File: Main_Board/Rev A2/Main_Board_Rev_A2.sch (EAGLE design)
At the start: 209 parts, among them J1 90814-0208, J2 90814-0206, J3 90814-0208, K1 G6K-2G-Y, K2 G6K-2G-Y, K3 G6K-2G-Y, K4 G6K-2G-Y, SW1 B3FS-1015, SW2 B3FS-1015, T1 MMBT2222AL, U1 LT1767EMS8E-5PBF, U10 SN74LVC2G17DBVR, U11 MCP2561-E/SN, U12 TLV313, U13 SN74LVC3G17DCTR, U2 TPL0401A, U3 SN74LVC3G17DCTR, U4 SN74LVC3G17DCTR, U5 TC1264-3.3, U6 DP83848JSQ/NOPB, U7 LPC1768FBD100, U8 AT24C512C-SSHM-B, U9 SN74LVC2G17DBVR, X1 22-05-7028-02, X10 22-05-7048-04, X11 5504F1-09S-02A-03, X12 22-05-7028-02, X13 22-05-7028-02, X14 22-05-7038-03, X15 22-05-7038-03, X16 22-05-7048-04, X17 22-05-7048-04, X18 22-05-7058-05, X2 22-27-2061-06, X3 RB1-125BAG1A, X4 MSTBA2, X5 22-05-7028-02, X6 USB3075-30-A, X7 FTSH-105-01-L-DV, X8 22-05-7028-02, X9 1241050-5

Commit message: Update schematic
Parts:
- removed C100: 4.7uF, rcl:CPOL-EUCT3216
- removed C111, C115, C118, C119, C123, C124, C125, C126, C135, C137, C138, C139, C140: 0.1uF, rcl:C-EUC0603
- removed C121: 10uF, rcl:CPOL-EUCT3216
- removed C127, C128: 18pF, rcl:C-EUC0603
- removed C136: 100nF, rcl:C-EUC0603
- removed D1: USB120, diode:USB120
- removed L100: 0603PS-103KLB, coilcraft:0603PS
- removed R100, R101: 0R, rcl:R-EU_R0603
- removed R102, R103: 10K, rcl:R-EU_R0603
- removed R104: 1K2, rcl:R-EU_R0603
- removed R105, R106, R107: 4K7, rcl:R-EU_R0603
- removed R60, R61: 1K, rcl:R-EU_R0603
- removed R62, R66: 100, rcl:R-EU_R0603
- removed SJ1, SJ2, SJ3: SOLDERJUMPERNO, SparkFun-Passives:SOLDERJUMPERNO
- removed TP3: TPB1,27, testpad:TPB1,27
- removed U$1: 3000, keystone:3000
- removed U13: SN74LVC3G17DCTR, ti:SN74LVC3G17DCTR
- removed X10, X16, X17: 22-05-7048-04, con-molex:22-05-7048-04
- removed X11: 5504F1-09S-02A-03, con-multicomp:5504F1-09S-02A-03
- removed X18: 22-05-7058-05, con-molex:22-05-7058-05
- removed X9: 1241050-5, con-amp:1241050-5
- removed XT1: ASE_50, crystal:ASE
- removed XT2: FC-135, crystal:FC-135
- removed XT3: ASE-12, crystal:ASE
- added C22: 100nF, rcl:C-EUC0603
- added C23: 4700pF, rcl:C-EUC0603
- added C24: 22uF, rcl:C-EUC0805
- added C25, C28, C29, C30, C31, C32, C33, C34, C36, C37, C38: 0.1uF, rcl:C-EUC0603
- added C26, C27: 18pF, rcl:C-EUC0603
- added C35: 10uF, rcl:CPOL-EUCT3216
- added D3: MBRS140, diode:MBRS140
- added GND: DP83848JSQ/NOPB, textas:DP83848JSQ/NOPB
- added J12: 22-27-2061-06, con-molex:22-27-2061-06
- added J15: 1241050-5, con-amp:1241050-5
- added J4: 5504F1-09S-02A-03, con-multicomp:5504F1-09S-02A-03
- added J5, J6, J8: 22-05-7048-04, con-molex:22-05-7048-04
- added J7: 22-05-7058-05, con-molex:22-05-7058-05
- added JP6: FIDUCIAL1X2, SparkFun:FIDUCIAL1X2
- added L2: 15uH, Wurth-POWER_MAGNETICS-rev16f:WE-PD2_5848/5820
- added L3: 0603PS-103KLB, coilcraft:0603PS
- added LED10: Blue, led:LEDCHIPLED_0603
- added P1: RB1-125BAG1A, con-wiznet:RB1-125BAG1A
- added R67, R68, R69: 0R, rcl:R-EU_R0603
- added R70: 1K5, rcl:R-EU_R0603
- added R71, R73, R76: 2K7, rcl:R-EU_R0603
- added R72, R74, R75: 1K, rcl:R-EU_R0603
- added R77, R78: 1K8, rcl:R-EU_R0603
- added R79, R80: 1K2, rcl:R-EU_R0603
- added TP5: TPB1,27, testpad:TPB1,27
- C1: MPN (none) -> GRT188R61H225KE13D; OC_NEWARK (none) -> 01AC8938
- C12: value 0.1uF -> 22uF; device rcl:C-EUC0603 -> rcl:C-EUC0805; MPN (none) -> MCMT21N220F250CT; OC_NEWARK (none) -> 23T7233
- C13: value 4700pF -> 100nF; MPN (none) -> MC0603B104K250CT; OC_NEWARK (none) -> 06R4925
- C14, C16, C18, C19, C20, C21, C7, C8: MPN (none) -> MC0603B104K250CT; OC_NEWARK (none) -> 06R4925
- C15, C17: MPN (none) -> F931A106MAA; OC_NEWARK (none) -> 58R3260
- C2: value 0.1uF -> 2.2uF; MPN (none) -> GRT188R61H225KE13D; OC_NEWARK (none) -> 01AC8938
- C3: value 0.1uF -> 1000pF; MPN (none) -> MC0603B102K500CT; OC_NEWARK (none) -> 06R4910
- C4: value 10uF -> 1000pF; device rcl:CPOL-EUCT3216 -> rcl:C-EUC0603; MPN (none) -> MC0603B102K500CT; OC_NEWARK (none) -> 06R4910
- C5, C6: value 1uF -> 2.2uF; MPN (none) -> GRT188R61H225KE13D; OC_FARNELL unknown -> (none); OC_NEWARK (none) -> 01AC8938
- C9: value 100nF -> 4.7uF; device rcl:C-EUC0603 -> rcl:CPOL-EUCT3216; MPN (none) -> F931A475MAA; OC_NEWARK (none) -> 58R3271
- D2: value CMDSH2-3 -> MBRS140; device diode:CMDSH2-3 -> diode:MBRS140; MF (none) -> ON SEMICONDUCTOR; MPN (none) -> MBRS140T3G; OC_NEWARK (none) -> 83H7272
- JP3, SW1, SW2: OC_NEWARK (none) -> unknown
- L1: value 4.7uF -> 10uH; device WE-PD:WE-PD-7447713047_1030/1050 -> Wurth-POWER_MAGNETICS-rev16f:WE-PD2_5848/5820; MPN (none) -> 74477410; OC_NEWARK (none) -> 08P2817
- LED3, LED4: MF MULTICOMP -> (none)
- R1: value 4K7 -> 1k5; MF (none) -> Multicomp Passives; MPN (none) -> MC0063W060311K5; OC_FARNELL (none) -> 2073391; OC_NEWARK (none) -> 58K4488
- R16: value 0R -> 1k5; MF (none) -> Multicomp Passives; MPN (none) -> MC0063W060311K5; OC_FARNELL (none) -> 2073391; OC_NEWARK (none) -> 58K4488
- R17: value 0R -> 4K7; MPN (none) -> MCMR06X4701FTL; OC_NEWARK (none) -> 86T3649
- R18: value 4K7 -> 220; MPN (none) -> MCMR06X2200FTL; OC_NEWARK (none) -> 86T3577
- R19: MPN (none) -> MCMR06X2200FTL; OC_NEWARK (none) -> 86T3577
- R20: value 220 -> 49.9; MPN (none) -> MCMR06X49R9FTL; OC_NEWARK (none) -> 86T3659
- R21, R22, R23: MPN (none) -> MCMR06X49R9FTL; OC_NEWARK (none) -> 86T3659
- R24: value 49.9 -> 4K7; MPN (none) -> MCMR06X4701FTL; OC_NEWARK (none) -> 86T3649
- R27: value 1K5 -> 4K7; MF MULTICOMP -> (none); MPN MCMR06X1501FTL -> MCMR06X4701FTL; OC_FARNELL 2073391 -> (none); OC_NEWARK 58K4488 -> 86T3649
- R28: value 4K7 -> 2K2; MPN (none) -> MCMR06X2201FTL; OC_NEWARK (none) -> 86T3578
- R29, R30: value 4K7 -> 31k6; MF (none) -> Multicomp Passives; MPN (none) -> MC0063W060311K5; OC_FARNELL (none) -> 2073391; OC_NEWARK (none) -> 58K4488
- R31: value 1K5 -> 10k; MF MULTICOMP -> (none); MPN MCMR06X1501FTL -> MCMR06X1002FTL; OC_NEWARK 58K4488 -> 86T3506
- R33: value 4K7 -> 52k3; MPN (none) -> MC0063W0603152K3; OC_FARNELL (none) -> 2073391; OC_NEWARK (none) -> 26M0962
- R49: value 1K2 -> 10k; MPN (none) -> MCMR06X1002FTL; OC_FARNELL (none) -> 2073391; OC_NEWARK (none) -> 86T3506
- R54, R55: MPN (none) -> MCMR06X60R4FTL; OC_NEWARK (none) -> 86T3680
- R56: value 1K8 -> 31k6; MF (none) -> Multicomp Passives; MPN (none) -> MC0063W060311K5; OC_FARNELL (none) -> 2073391; OC_NEWARK (none) -> 58K4488
- R57: value 1K8 -> 4K7; MPN (none) -> MCMR06X4701FTL; OC_NEWARK (none) -> 86T3649
- R58, R59: value 10K -> 1K; MPN (none) -> MCMR06X1001FTL; OC_NEWARK (none) -> 86T3505
- R63, R64: value 100 -> 10K; MPN (none) -> MCMR06X1002FTL; OC_NEWARK (none) -> 86T3506
- R65: value 100 -> 0R; MPN (none) -> MCMR06X000 PTL; OC_NEWARK (none) -> 86T3500
- U1: value LT1767EMS8E-5PBF -> LT3686HDDPBF; device lineartechnology:LT1767EMS8E-5PBF -> lineartechnology:LT3686HDDPBF
- U11: MPN (none) -> MCP2561-E/SN; OC_NEWARK (none) -> 12X8698
- U12: MPN (none) -> TLV313IDBVT; OC_NEWARK (none) -> 95Y0395
- U5: value TC1264-3.3 -> LT3686HDDPBF; device microchip-6:TC1264-3.3 -> lineartechnology:LT3686HDDPBF; OC_FARNELL unknown -> (none)
- U6: value DP83848JSQ/NOPB -> LPC1768FBD100; device texas:DP83848JSQ/NOPB -> NXP:LPC1768FBD100; MPN (none) -> LPC1768FBD100; OC_NEWARK (none) -> 15R1840
- U7: value LPC1768FBD100 -> AT24C512C-SSHM-B; device NXP:LPC1768FBD100 -> atmel:AT24C512C-SSHM-B
- U8: value AT24C512C-SSHM-B -> SN74LVC3G17DCTR; device atmel:AT24C512C-SSHM-B -> ti:SN74LVC3G17DCTR; MF (none) -> TEXAS INSTRUMENTS
- X1: value 22-05-7028-02 -> ASE_50; device con-molex:22-05-7028-02 -> crystal:ASE; MPN (none) -> ASE-50.000MHZ-LC-T; OC_NEWARK (none) -> 84R2105
- X2: value 22-27-2061-06 -> FC-135; device con-molex:22-27-2061-06 -> crystal:FC-135; MPN (none) -> Q13FC13500004; OC_NEWARK (none) -> 31M4970
- X3: value RB1-125BAG1A -> ASE-12; device con-wiznet:RB1-125BAG1A -> crystal:ASE; MPN (none) -> ASE-12.000MHZ-LC-T; OC_NEWARK (none) -> 40Y2118
- X7: value FTSH-105-01-L-DV -> 3000; device con-samtec:FTSH-105-01-L-DV -> keystone:3000; MF (none) -> KEYSTONE ELECTR; MPN (none) -> 3000; OC_NEWARK (none) -> 66F5622
- renumbered C110 to C15, C112 to C20, C113 to C19, C114 to C16, C116 to C14, C117 to C18, C120 to C21, C122 to C17
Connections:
- removed net CAN_H: R54.2, U11.CANH, X11C.7
- removed net CAN_L: R55.1, U11.CANL, X11C.2
- removed net ETH_RXD_N: U6.RXD_1/PHYAD2, U7.P1[9]/ENET_RXD0
- removed net ETH_RXD_P: U6.RXD_0/PHYAD1, U7.P1[10]/ENET_RXD1
- removed net ETH_TXD_N: U6.TXD_0, U7.P1[0]/ENET_TXD0
- removed net ETH_TXD_P: U6.TXD_1, U7.P1[1]/ENET_TXD1
- removed net N$67: R104.2, R56.2, U12.-IN
- removed net N$68: R56.1, X10-3.S
- removed net N$69: SJ1.1, X2-2.S
- removed net RESET: R103.1, R16.1, SW1.1, U7.*RESET, X7-10.S, X9.P$5
- new net !JTAG_TRST: J15.P$5, U6.*TRST
- new net !RESET: R63.1, R65.1, SW1.1, U6.*RESET
- new net CAN_N: J4C.2, R55.1, U11.CANL
- new net CAN_P: J4C.7, R54.2, U11.CANH
- new net ETH_RXD_0: GND.RXD_0/PHYAD1, U6.P1[9]/ENET_RXD0
- new net ETH_RXD_1: GND.RXD_1/PHYAD2, U6.P1[10]/ENET_RXD1
- new net ETH_TXD_0: GND.TXD_0, U6.P1[0]/ENET_TXD0
- new net ETH_TXD_1: GND.TXD_1, U6.P1[1]/ENET_TXD1
- new net LED_DEBUG: LED10.A, U6.P1[21]/*MCABORT/PWM1[3]/SSEL0
- new net N$10: R30.2, U1.RT
- new net N$30: R31.2, R33.1, U5.FB
- new net N$34: C5.2, D2.C, L2.1, U5.SW
- new net N$36: R49.2, R56.1, U1.FB
- new net N$78: J8-3.S, R78.1
- new net N$79: R77.2, R79.2, U12.+IN
- new net N$80: R78.2, R80.2, U12.-IN
- net +24V: now also C2.1, J4C.9, J5-1.S, J6-1.S, U1.EN/UVLO, U5.EN/UVLO, U5.VIN; no longer X11C.9, X16-1.S, X17-1.S
- net +3V3: now also C22.1, C25.1, C29.1, C30.1, C31.1, C32.1, C33.1, C34.1, C35.+, C36.1, C37.1, C38.1, C9.+, GND.AVDD33, GND.IOVDD33, GND.IOVDD33_2, J15.P$1, L1.2, L3.1, P1.CT, R1.2, R17.2, R18.2, R20.1, R27.2, R56.2, R57.2, R63.2, R64.2, TP5.TP, U1.BD, U6.NC, U6.VDD, U6.VDD_2, U6.VDD_3, U6.VDD_4, U6.VDD_5, U6.VDD_6, U7.VCC, X1.TRI, X1.VDD, X3.TRI, X3.VDD; no longer C100.+, C111.1, C115.1, C118.1, C119.1, C121.+, C123.1, C124.1, C125.1, C135.1, C136.1, C137.1, C6.1, C9.1, L100.1, R102.2, R103.2, R20.2, R24.1, R29.2, R30.2, R31.2, R33.2, R58.2, R59.2, TP3.TP, U11.VDD, U13.VCC, U5.VOUT, U6.AVDD33, U6.IOVDD33, U6.IOVDD33_2, U7.NC, U7.VDD, U7.VDD_2, U7.VDD_3, U7.VDD_4, U7.VDD_5, U7.VDD_6, X3.CT, X7-1.S, X9.P$1, XT1.TRI, XT1.VDD, XT3.TRI, XT3.VDD
- net +5V: now also C13.1, C24.1, J7-4.S, J8-1.S, L2.2, R16.2, R33.2, R71.1, R73.1, R76.1, U11.VDD, U5.BD; no longer C4.+, C5.1, D2.A, L1.2, R105.1, R106.1, R107.1, R27.2, SJ1.2, U1.FB, U5.VIN, X1-1.S, X10-1.S, X18-1.S
- net ADC_SLACK_DETECTION: now also R80.1, U6.P0[25]/AD0[2]/I2SRX_SDA/TXD3; no longer R49.1, U7.P0[25]/AD0[2]/I2SRX_SDA/TXD3
- net ADC_TEMP_0: now also U6.P0[23]/AD0[0]/I2SRX_CLK/CAP3[0]; no longer U7.P0[23]/AD0[0]/I2SRX_CLK/CAP3[0]
- net ADC_TEMP_1: now also U6.P0[24]/AD0[1]/I2SRX_WS/CAP3[1]; no longer U7.P0[24]/AD0[1]/I2SRX_WS/CAP3[1]
- net AVDD: now also C28.1, L3.2, U6.VDDA, U6.VREFP; no longer C126.1, L100.2, U7.VDDA, U7.VREFP
- net BOOT_SELECT_P2_10: now also R68.1, U6.P2[10]/*EINT0/NMI; no longer R100.1, U7.P2[10]/*EINT0/NMI
- net BOOT_SELECT_P2_12: now also R69.1, U6.P2[12]/*EINT2/I2STX_WS; no longer R101.1, U7.P2[12]/*EINT2/I2STX_WS
- net BRAKE_SENSOR_1: now also U6.P0[4]/I2SRX_CLK/RD2/CAP2[0]; no longer U7.P0[4]/I2SRX_CLK/RD2/CAP2[0]
- net BRAKE_SENSOR_2: now also U6.P0[5]/I2SRX_WS/TD2/CAP2[1]; no longer U7.P0[5]/I2SRX_WS/TD2/CAP2[1]
- net CAN_RX: now also U6.P0[0]/RD1/TXD3/SDA1; no longer U7.P0[0]/RD1/TXD3/SDA1
- net CAN_SHLD: now also J4C.5; no longer X11C.5
- net CAN_SPLIT: now also C23.2; no longer C13.2
- net CAN_TX: now also U6.P0[1]/TD1/RXD3/SCL1; no longer U7.P0[1]/TD1/RXD3/SCL1
- net DRIVE_EN: now also U6.P0[6]/I2SRX_SDA/SSEL1/MAT2[0]; no longer U7.P0[6]/I2SRX_SDA/SSEL1/MAT2[0]
- net DRIVE_ERR: now also U6.P0[7]/I2STX_CLK/SCK1/MAT2[1]; no longer U7.P0[7]/I2STX_CLK/SCK1/MAT2[1]
- net EEPROM_SCL: now also R27.1, U6.P0[28]/SCL0/USB_SCL, U7.SCL; no longer R30.1, U7.P0[28]/SCL0/USB_SCL, U8.SCL
- net EEPROM_SDA: now also R17.1, U6.P0[27]/SDA0/USB_SDA, U7.SDA; no longer R33.1, U7.P0[27]/SDA0/USB_SDA, U8.SDA
- net ENCODER_A: now also U6.P1[20]/MCI0/PWM1[2]/SCK0, U8.1Y; no longer U13.1Y, U7.P1[20]/MCI0/PWM1[2]/SCK0
- net ENCODER_B: now also U6.P1[23]/MCI1/PWM1[4]/MISO0, U8.2Y; no longer U13.2Y, U7.P1[23]/MCI1/PWM1[4]/MISO0
- net ENCODER_Z: now also U6.P1[24]/MCI2/PWM1[5]/MOSI0, U8.3Y; no longer U13.3Y, U7.P1[24]/MCI2/PWM1[5]/MOSI0
- net ETH_CLK_EN: now also U6.P1[27]/CLKOUT/*USB_OVRCR/CAP0[1]; no longer U7.P1[27]/CLKOUT/*USB_OVRCR/CAP0[1]
- net ETH_CRS: now also GND.CRS/CRS_DV/LED_CFG, U6.P1[8]/ENET_CRS; no longer U6.CRS/CRS_DV/LED_CFG, U7.P1[8]/ENET_CRS
- net ETH_MDC: now also GND.MDC, U6.P1[16]/ENET_MDC; no longer U6.MDC, U7.P1[16]/ENET_MDC
- net ETH_MDIO: now also GND.MDIO, U6.P1[17]/ENET_MDIO; no longer U6.MDIO, U7.P1[17]/ENET_MDIO
- net ETH_RST: now also GND.RESET_N, U6.P1[28]/MCOA2/PCAP1[0]/MAT0[0]; no longer U6.RESET_N
- net ETH_RX_ER: now also GND.RX_ER/MDIX_EN, U6.P1[14]/ENET_RX_ER; no longer U6.RX_ER/MDIX_EN, U7.P1[14]/ENET_RX_ER
- net ETH_RX_N: now also GND.RD-, P1.RD-, R23.2; no longer R24.2, U6.RD-, X3.RD-
- net ETH_RX_P: now also GND.RD+, P1.RD+, R22.2; no longer R23.2, U6.RD+, X3.RD+
- net ETH_TXD_EN: now also GND.TX_EN, U6.P1[4]/ENET_TX_EN; no longer U6.TX_EN, U7.P1[4]/ENET_TX_EN
- net ETH_TX_N: now also GND.TD-, P1.TD-, R21.2; no longer R22.2, U6.TD-, X3.TD-
- net ETH_TX_P: now also GND.TD+, P1.TD+, R20.2; no longer R21.2, U6.TD+, X3.TD+
- net ETH_X1: now also GND.X1, U6.P1[15]/ENET_REF_CLK, X1.OUT; no longer U6.X1, XT1.OUT
- net FAN_1_PWM: now also R58.2, U6.P2[0]/PWM1[1]/TXD1; no longer R61.2, U7.P2[0]/PWM1[1]/TXD1
- net FAN_1_SENSOR: now also U6.P0[8]/I2STX_WS/MISO1/MAT2[2]; no longer R59.1, R62.2
- net FAN_2_PWM: now also R59.2, U6.P2[1]/PWM1[2]/RXD1; no longer R60.2, U7.P2[1]/PWM1[2]/RXD1
- net FAN_2_SENSOR: now also U6.P0[9]/I2STX_SDA/MOSI1/MAT2[3]; no longer R58.1, R66.2
- net GND: now also C13.2, C2.2, C22.2, C24.2, C25.2, C26.2, C27.2, C28.2, C29.2, C3.2, C30.2, C31.2, C32.2, C33.2, C34.2, C35.-, C36.2, C37.2, C38.2, C4.2, C9.-, GND.AGND, GND.AGND_2, GND.DAP, GND.DGND, GND.IOGND, J12-1.S, J15.P$2, J4C.3, J4C.6, J5-4.S, J6-4.S, J7-1.S, J8-4.S, P1.R4, P1.R5, P1.R6, R24.2, R29.1, R30.1, R31.1, R49.1, R70.2, R79.1, U1.EP, U1.MODE, U5.EP, U5.MODE, U6.VREFN, U6.VSS, U6.VSSA, U6.VSS_2, U6.VSS_3, U6.VSS_4, U6.VSS_5, U6.VSS_6, U7.A0, U7.A1, U7.A2, U7.GND, X1.GND, X3.GND, X7.VBAT-; no longer C100.-, C111.2, C115.2, C118.2, C119.2, C121.-, C123.2, C124.2, C125.2, C126.2, C127.2, C128.2, C135.2, C136.2, C137.2, C138.2, C139.2, C140.2, C4.-, C5.2, C6.2, C9.2, D1.A, R1.1, R104.1, R18.2, SJ2.2, SJ3.2, U$1.VBAT-, U1.GND, U1.GND_2, U1.SYNC, U13.GND, U5.GND, U5.GND_2, U6.AGND, U6.AGND_2, U6.DAP, U6.DGND, U6.IOGND, U7.VREFN, U7.VSS, U7.VSSA, U7.VSS_2, U7.VSS_3, U7.VSS_4, U7.VSS_5, U7.VSS_6, U8.A0, U8.A1, U8.A2, X1-2.S, X10-4.S, X11C.3, X11C.6, X16-4.S, X17-4.S, X2-1.S, X3.R4, X3.R5, X3.R6, X7-3.S, X7-5.S, X7-9.S, X9.P$2, XT1.GND, XT3.GND
- net HMI_BUTTON_CPU_1: now also U6.P0[16]/RXD1/SSEL0/SSEL; no longer U7.P0[16]/RXD1/SSEL0/SSEL
- net HMI_BUTTON_CPU_2: now also U6.P0[15]/TXD1/SCK0/SCK; no longer U7.P0[15]/TXD1/SCK0/SCK
- net HMI_BUTTON_CPU_3: now also U6.P0[17]/CTS1/MISO0/MISO; no longer U7.P0[17]/CTS1/MISO0/MISO
- net HMI_BUTTON_CPU_4: now also U6.P0[18]/DCD1/MOSI0/MOSI; no longer U7.P0[18]/DCD1/MOSI0/MOSI
- net HMI_BUTTON_CPU_5: now also U6.P0[19]/DSR1/SDA1; no longer U7.P0[19]/DSR1/SDA1
- net HMI_BUTTON_CPU_6: now also R65.2, R67.1; no longer R16.2, R17.1
- net HMI_BUTTON_MCU_FCT_6: now also R67.2, U6.P0[20]/DTR1/SCL1; no longer R17.2, U7.P0[20]/DTR1/SCL1
- net HMI_LCD_BACKLIGHT: now also U6.P0[22]/RTS1/TD1; no longer U7.P0[22]/RTS1/TD1
- net HMI_LCD_SCL: now also U6.P0[11]/RXD2/SCL2/MAT3[1]; no longer U7.P0[11]/RXD2/SCL2/MAT3[1]
- net HMI_LCD_SDA: now also U6.P0[10]/TXD2/SDA2/MAT3[0]; no longer U7.P0[10]/TXD2/SDA2/MAT3[0]
- net HMI_LED_1: now also U6.P2[2]/PWM1[3]/CTS1/TRACEDATA[3]; no longer U7.P2[2]/PWM1[3]/CTS1/TRACEDATA[3]
- net HMI_LED_2: now also U6.P2[3]/PWM1[4]/DCD1/TRACEDATA[2]; no longer U7.P2[3]/PWM1[4]/DCD1/TRACEDATA[2]
- net HMI_LED_3: now also U6.P2[4]/PWM1[5]/DSR1/TRACEDATA[1]; no longer U7.P2[4]/PWM1[5]/DSR1/TRACEDATA[1]
- net HMI_LED_4: now also U6.P2[5]/PWM1[6]/DTR1/TRACEDATA[0]; no longer U7.P2[5]/PWM1[6]/DTR1/TRACEDATA[0]
- net ISP_RXDO: now also J12-4.S, J15.P$3, U6.P0[3]/RXD0/AD0[6]; no longer U7.P0[3]/RXD0/AD0[6], X2-4.S
- net ISP_TXDO: now also J12-5.S, J15.P$4, U6.P0[2]/TXD0/AD0[7]; no longer U7.P0[2]/TXD0/AD0[7], X2-5.S
- net JTAG_TCK: now also J15.P$8, U6.TCK/SWDCLK; no longer U7.TCK/SWDCLK, X7-4.S, X9.P$8
- net JTAG_TDI: now also J15.P$7, U6.TDI; no longer U7.TDI, X7-8.S, X9.P$7
- net JTAG_TDO: now also J15.P$9, U6.TDO/SWO; no longer U7.TDO/SWO, X7-6.S, X9.P$9
- net JTAG_TMS: now also J15.P$10, U6.TMS/SWDIO; no longer U7.TMS/SWDIO, X7-2.S, X9.P$10
- net L1_1: now also GND.LED_LINK/AN0, P1.L2; no longer U6.LED_LINK/AN0, X3.L2
- net L1_2: now also GND.LED_SPEED/AN1, P1.L4; no longer U6.LED_SPEED/AN1, X3.L4
- net MII_MODE: now also GND.RX_DV/MII_MODE; no longer U6.RX_DV/MII_MODE
- net N$11: now also J5-2.S, R58.1; no longer R61.1, X17-2.S
- net N$12: now also J7-3.S, R71.2, R72.1; no longer R66.1, X16-3.S
- net N$13: now also J6-2.S, R59.1; no longer R60.1, X16-2.S
- net N$14: now also J7-5.S, R74.1, R76.2; no longer R62.1, X17-3.S
- net N$15: no longer R38.2
- net N$16: now also R38.2
- net N$22: now also C4.1, U1.SS; no longer JP3.1, R29.1, U8.WP
- net N$3: now also C23.1; no longer C13.1
- net N$31: now also C5.1, U5.BOOST; no longer R57.1, X10-2.S
- net N$35: now also D2.A, U5.DA; no longer R107.2, R63.1, X18-2.S
- net N$4: now also GND.RBIAS, R24.1; no longer R18.1, U6.RBIAS
- net N$40: now also C6.1, U1.BOOST; no longer R106.2, R64.1, X18-3.S
- net N$43: now also C6.2, D3.C, L1.1, U1.SW; no longer C2.2, D2.C, U1.BOOST
- net N$46: now also D3.A, U1.DA; no longer R105.2, R65.1, X18-4.S
- net N$47: now also JP3.1, R57.1, U7.WP; no longer C3.1, R1.2
- net N$48: now also R64.1, R68.2, R69.2, SW2.1; no longer C3.2, U1.VC
- net N$49: now also LED10.C, R70.1; no longer C2.1, D1.C, L1.1, U1.SW
- net N$5: now also R29.2, U5.RT; no longer R100.2, R101.2, R102.1, SW2.1
- net N$50: now also R1.1; no longer R31.1
- net N$51: now also R16.1; no longer R27.1
- net N$52: now also J7-2.S, R73.2, R75.1; no longer C138.1, R65.2, U13.3A
- net N$53: now also R75.2, U8.3A; no longer C139.1, R64.2, U13.2A
- net N$54: now also R74.2, U8.2A; no longer C140.1, R63.2, U13.1A
- net N$6: now also C3.1, U5.SS; no longer SJ2.1, SJ3.1, X11S.SHIELD
- net N$61: now also R72.2, U8.1A; no longer R49.2, R57.2, U12.+IN
- net N$62: now also J8-2.S, R77.1; no longer X18-5.S
- net N$8: now also P1.L1, R19.1; no longer R20.1, X3.L1
- net N$9: now also P1.L3, R18.1; no longer R19.1, X3.L3
- net PFBOUT: now also GND.PFBIN1, GND.PFBIN2, GND.PFBOUT; no longer U6.PFBIN1, U6.PFBIN2, U6.PFBOUT
- net RTCX1: now also C26.1, U6.RTCX1, X2.1; no longer C127.1, U7.RTCX1, XT2.1
- net RTCX2: now also C27.1, U6.RTCX2, X2.2; no longer C128.1, U7.RTCX2, XT2.2
- net USB_D_N: now also R36.2, U6.P0[30]/USB_D?; no longer R35.2, U7.P0[30]/USB_D?
- net USB_D_P: now also R35.2, U6.P0[29]/USB_D+; no longer R36.2, U7.P0[29]/USB_D+
- net USB_UP_LED: now also U6.P1[18]/USB_UP_LED/PWM1[1]/CAP1[0]; no longer U7.P1[18]/USB_UP_LED/PWM1[1]/CAP1[0]
- net USB_V_BUS: now also U6.P1[30]/VBUS/AD0[4]; no longer U7.P1[30]/VBUS/AD0[4]
- net VBAT+: now also U6.VBAT, X7.VBAT+; no longer U$1.VBAT+, U7.VBAT
- net XTAL1: now also U6.XTAL1, X3.OUT; no longer U7.XTAL1, XT3.OUT
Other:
- note removed: "UART"

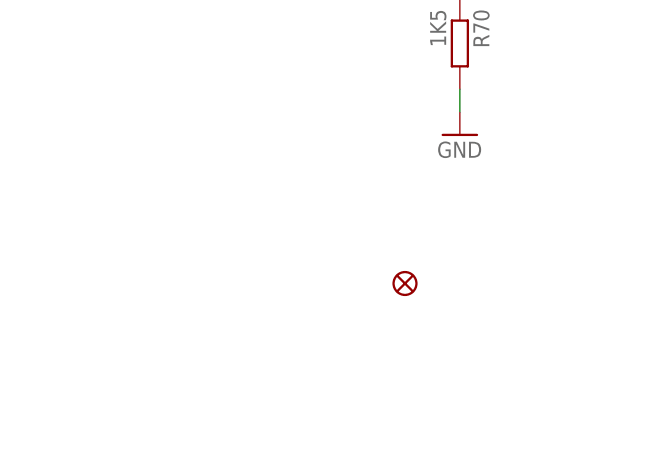
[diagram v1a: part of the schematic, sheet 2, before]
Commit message: Place component on the board
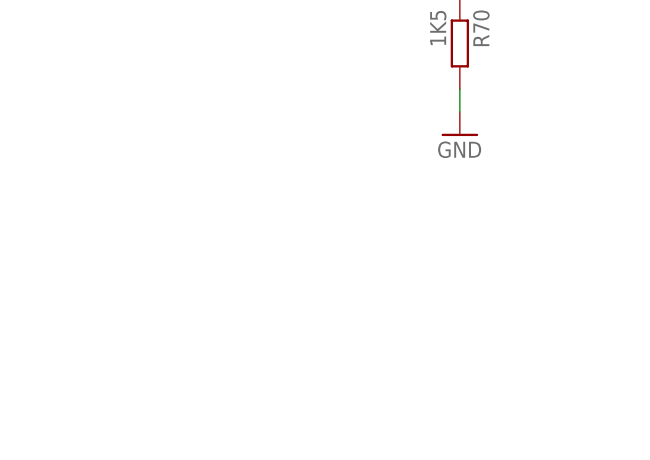
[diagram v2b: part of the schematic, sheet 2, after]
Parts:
- removed JP6: FIDUCIAL1X2, SparkFun:FIDUCIAL1X2
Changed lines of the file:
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@@
 </part>
 <part name="GND87" library="supply1" deviceset="GND" device=""/>
-<part name="JP6" library="SparkFun" deviceset="FIDUCIAL" device="1X2">
-<attribute name="MF" value=""/>
-<attribute name="MPN" value=""/>
-<attribute name="OC_NEWARK" value="unknown"/>
-</part>
 <part name="J12" library="con-molex" deviceset="22-?-06" device="27-2061">
 <attribute name="MF" value="MOLEX"/>
@@
 </instance>
 <instance part="GND87" gate="1" x="358.14" y="35.56"/>
-<instance part="JP6" gate="G$1" x="352.044" y="19.05">
-<attribute name="OC_NEWARK" x="352.044" y="19.05" size="1.778" layer="96" display="off"/>
-<attribute name="MF" x="352.044" y="19.05" size="1.778" layer="96" display="off"/>
-<attribute name="MPN" x="352.044" y="19.05" size="1.778" layer="96" display="off"/>
-</instance>
 </instances>
 <busses>

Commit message: Route Ethernet on the main board
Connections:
- removed net FAN_1_SENSOR: U6.P0[8]/I2STX_WS/MISO1/MAT2[2]
- removed net FAN_2_SENSOR: U6.P0[9]/I2STX_SDA/MOSI1/MAT2[3]
- net FAN_1_PWM: now also U6.P3[25]/MAT0[0]/PWM1[2]; no longer U6.P2[0]/PWM1[1]/TXD1
- net FAN_2_PWM: now also U6.P3[26]/STCLK/MAT0[1]/PWM1[3]; no longer U6.P2[1]/PWM1[2]/RXD1
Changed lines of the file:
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@@
 <net name="FAN_1_PWM" class="1">
 <segment>
-<pinref part="U6" gate="A" pin="P2[0]/PWM1[1]/TXD1"/>
-<wire x1="317.5" y1="167.64" x2="322.58" y2="167.64" width="0.1524" layer="91"/>
-<label x="322.58" y="167.64" size="1.27" layer="95" xref="yes"/>
+<wire x1="134.62" y1="165.1" x2="127" y2="165.1" width="0.1524" layer="91"/>
+<label x="127" y="165.1" size="1.27" layer="95" rot="R180" xref="yes"/>
+<pinref part="U6" gate="A" pin="P3[25]/MAT0[0]/PWM1[2]"/>
 </segment>
 </net>
 <net name="FAN_2_PWM" class="1">
 <segment>
-<pinref part="U6" gate="A" pin="P2[1]/PWM1[2]/RXD1"/>
-<wire x1="317.5" y1="165.1" x2="322.58" y2="165.1" width="0.1524" layer="91"/>
-<label x="322.58" y="165.1" size="1.27" layer="95" xref="yes"/>
-<wire x1="317.5" y1="165.1" x2="322.58" y2="165.1" width="0.1524" layer="91"/>
+<label x="127" y="167.64" size="1.27" layer="95" rot="R180" xref="yes"/>
+<wire x1="132.08" y1="167.64" x2="127" y2="167.64" width="0.1524" layer="91"/>
+<pinref part="U6" gate="A" pin="P3[26]/STCLK/MAT0[1]/PWM1[3]"/>
+<wire x1="132.08" y1="167.64" x2="134.62" y2="167.64" width="0.1524" layer="91"/>
 </segment>
 </net>
@@
 </segment>
 </net>
-<net name="FAN_1_SENSOR" class="1">
-<segment>
-<pinref part="U6" gate="A" pin="P0[8]/I2STX_WS/MISO1/MAT2[2]"/>
-<wire x1="317.5" y1="172.72" x2="322.58" y2="172.72" width="0.1524" layer="91"/>
-<label x="322.58" y="172.72" size="1.27" layer="95" xref="yes"/>
-</segment>
-</net>
-<net name="FAN_2_SENSOR" class="1">
-<segment>
-<pinref part="U6" gate="A" pin="P0[9]/I2STX_SDA/MOSI1/MAT2[3]"/>
-<wire x1="317.5" y1="170.18" x2="322.58" y2="170.18" width="0.1524" layer="91"/>
-<label x="322.58" y="170.18" size="1.27" layer="95" xref="yes"/>
-</segment>
-</net>

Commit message: Route CAN
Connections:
- net CAN_RX renamed CAN_X_N
- net CAN_TX renamed CAN_X_P
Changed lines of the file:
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@@
 </segment>
 </net>
-<net name="CAN_RX" class="1">
+<net name="CAN_X_N" class="1">
 <segment>
 <pinref part="U11" gate="G$1" pin="RXD"/>
@@
 </segment>
 </net>
-<net name="CAN_TX" class="1">
+<net name="CAN_X_P" class="1">
 <segment>
 <pinref part="U11" gate="G$1" pin="TXD"/>
@@
 </busses>
 <nets>
-<net name="CAN_RX" class="1">
+<net name="CAN_X_N" class="1">
 <segment>
 <pinref part="U6" gate="A" pin="P0[0]/RD1/TXD3/SDA1"/>
@@
 </segment>
 </net>
-<net name="CAN_TX" class="1">
+<net name="CAN_X_P" class="1">
 <segment>
 <pinref part="U6" gate="A" pin="P0[1]/TD1/RXD3/SCL1"/>

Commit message: Route the board
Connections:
- net +3V3: now also LED10.A
- net ADC_SLACK_DETECTION: now also U6.P0[23]/AD0[0]/I2SRX_CLK/CAP3[0]; no longer U6.P0[25]/AD0[2]/I2SRX_SDA/TXD3
- net ADC_TEMP_0: now also U6.P0[25]/AD0[2]/I2SRX_SDA/TXD3; no longer U6.P0[23]/AD0[0]/I2SRX_CLK/CAP3[0]
- net GND: no longer R70.2
- net LED_DEBUG: now also R70.2; no longer LED10.A
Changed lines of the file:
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@@
 <attribute name="OC_NEWARK" value="86T3542"/>
 </part>
-<part name="GND87" library="supply1" deviceset="GND" device=""/>
 <part name="J12" library="con-molex" deviceset="22-?-06" device="27-2061">
 <attribute name="MF" value="MOLEX"/>
@@
 <part name="GND97" library="supply1" deviceset="GND" device=""/>
 <part name="+3V28" library="supply1" deviceset="+3V3" device=""/>
+<part name="+3V14" library="supply1" deviceset="+3V3" device=""/>
 </parts>
 <sheets>
@@
 <attribute name="MPN" x="358.14" y="45.72" size="1.778" layer="96" display="off"/>
 </instance>
-<instance part="GND87" gate="1" x="358.14" y="35.56"/>
+<instance part="+3V14" gate="G$1" x="358.14" y="66.04"/>
 </instances>
 <busses>
@@
 <pinref part="+3V16" gate="G$1" pin="+3V3"/>
 <wire x1="60.96" y1="137.16" x2="60.96" y2="152.4" width="0.1524" layer="91"/>
+</segment>
+<segment>
+<pinref part="LED10" gate="G$1" pin="A"/>
+<pinref part="+3V14" gate="G$1" pin="+3V3"/>
+<wire x1="358.14" y1="60.96" x2="358.14" y2="63.5" width="0.1524" layer="91"/>
 </segment>
 </net>
@@
 <pinref part="GND86" gate="1" pin="GND"/>
 </segment>
-<segment>
-<pinref part="R70" gate="G$1" pin="2"/>
-<wire x1="358.14" y1="40.64" x2="358.14" y2="38.1" width="0.1524" layer="91"/>
-<pinref part="GND87" gate="1" pin="GND"/>
-</segment>
 </net>
 <net name="ETH_CLK_EN" class="1">
@@
 <net name="ADC_TEMP_0" class="1">
 <segment>
-<pinref part="U6" gate="A" pin="P0[23]/AD0[0]/I2SRX_CLK/CAP3[0]"/>
-<wire x1="134.62" y1="210.82" x2="127" y2="210.82" width="0.1524" layer="91"/>
-<label x="127" y="210.82" size="1.27" layer="95" rot="R180" xref="yes"/>
+<wire x1="134.62" y1="215.9" x2="124.46" y2="215.9" width="0.1524" layer="91"/>
+<label x="124.46" y="215.9" size="1.27" layer="95" rot="R180" xref="yes"/>
+<pinref part="U6" gate="A" pin="P0[25]/AD0[2]/I2SRX_SDA/TXD3"/>
 </segment>
 </net>
 <net name="ADC_TEMP_1" class="1">
 <segment>
+<wire x1="134.62" y1="213.36" x2="124.46" y2="213.36" width="0.1524" layer="91"/>
+<label x="124.46" y="213.36" size="1.27" layer="95" rot="R180" xref="yes"/>
 <pinref part="U6" gate="A" pin="P0[24]/AD0[1]/I2SRX_WS/CAP3[1]"/>
-<wire x1="134.62" y1="213.36" x2="127" y2="213.36" width="0.1524" layer="91"/>
-<label x="127" y="213.36" size="1.27" layer="95" rot="R180" xref="yes"/>
 </segment>
 </net>
@@
 <net name="ADC_SLACK_DETECTION" class="1">
 <segment>
-<pinref part="U6" gate="A" pin="P0[25]/AD0[2]/I2SRX_SDA/TXD3"/>
-<wire x1="134.62" y1="215.9" x2="127" y2="215.9" width="0.1524" layer="91"/>
-<label x="127" y="215.9" size="1.27" layer="95" rot="R180" xref="yes"/>
+<wire x1="134.62" y1="210.82" x2="124.46" y2="210.82" width="0.1524" layer="91"/>
+<label x="124.46" y="210.82" size="1.27" layer="95" rot="R180" xref="yes"/>
+<pinref part="U6" gate="A" pin="P0[23]/AD0[0]/I2SRX_CLK/CAP3[0]"/>
 </segment>
 </net>
@@
 <net name="LED_DEBUG" class="1">
 <segment>
-<pinref part="LED10" gate="G$1" pin="A"/>
-<wire x1="358.14" y1="63.5" x2="358.14" y2="60.96" width="0.1524" layer="91"/>
-<wire x1="358.14" y1="63.5" x2="348.996" y2="63.5" width="0.1524" layer="91"/>
-<label x="348.996" y="63.5" size="1.27" layer="95" rot="R180" xref="yes"/>
-</segment>
-<segment>
 <wire x1="134.62" y1="144.78" x2="127.254" y2="144.78" width="0.1524" layer="91"/>
 <pinref part="U6" gate="A" pin="P1[21]/*MCABORT/PWM1[3]/SSEL0"/>
 <label x="127" y="144.78" size="1.27" layer="95" rot="R180" xref="yes"/>
 </segment>
-</net>
+<segment>
+<wire x1="358.14" y1="38.1" x2="343.916" y2="38.1" width="0.1524" layer="91"/>
+<label x="343.916" y="38.1" size="1.27" layer="95" rot="R180" xref="yes"/>
+<pinref part="R70" gate="G$1" pin="2"/>
+<wire x1="358.14" y1="40.64" x2="358.14" y2="38.1" width="0.1524" layer="91"/>
+</segment>
+</net>

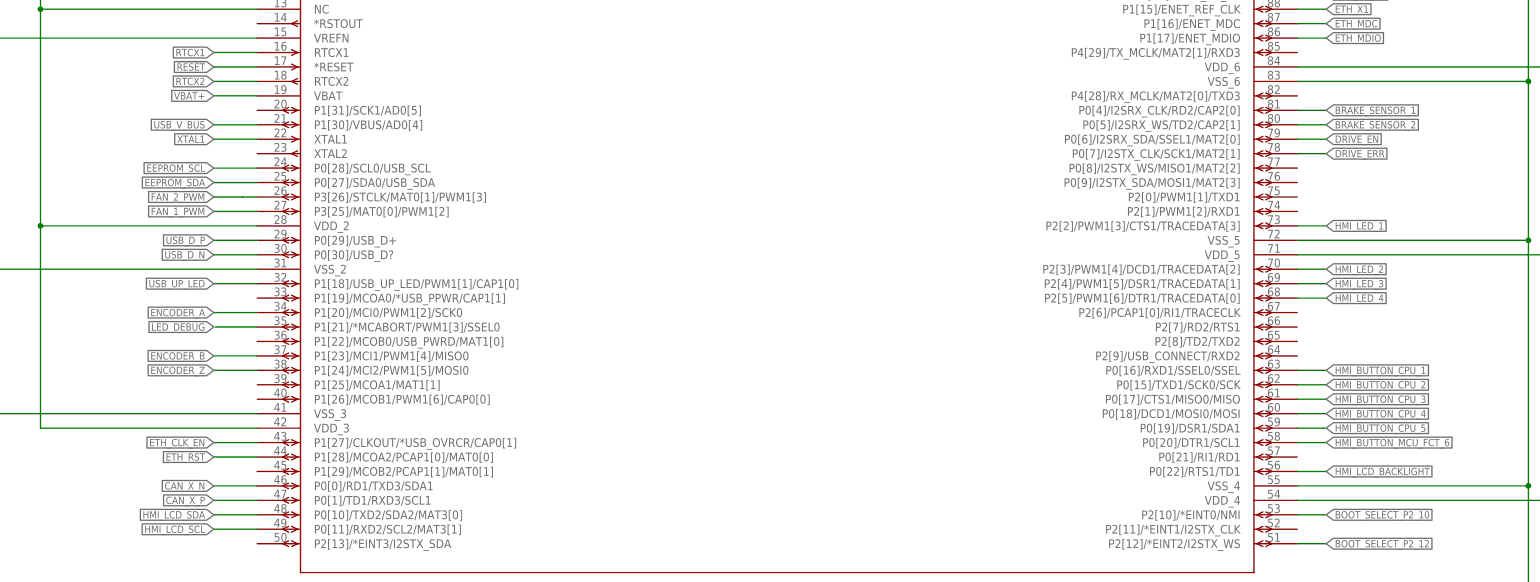
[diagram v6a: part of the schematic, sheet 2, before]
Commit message: Route all the signals (except power net)
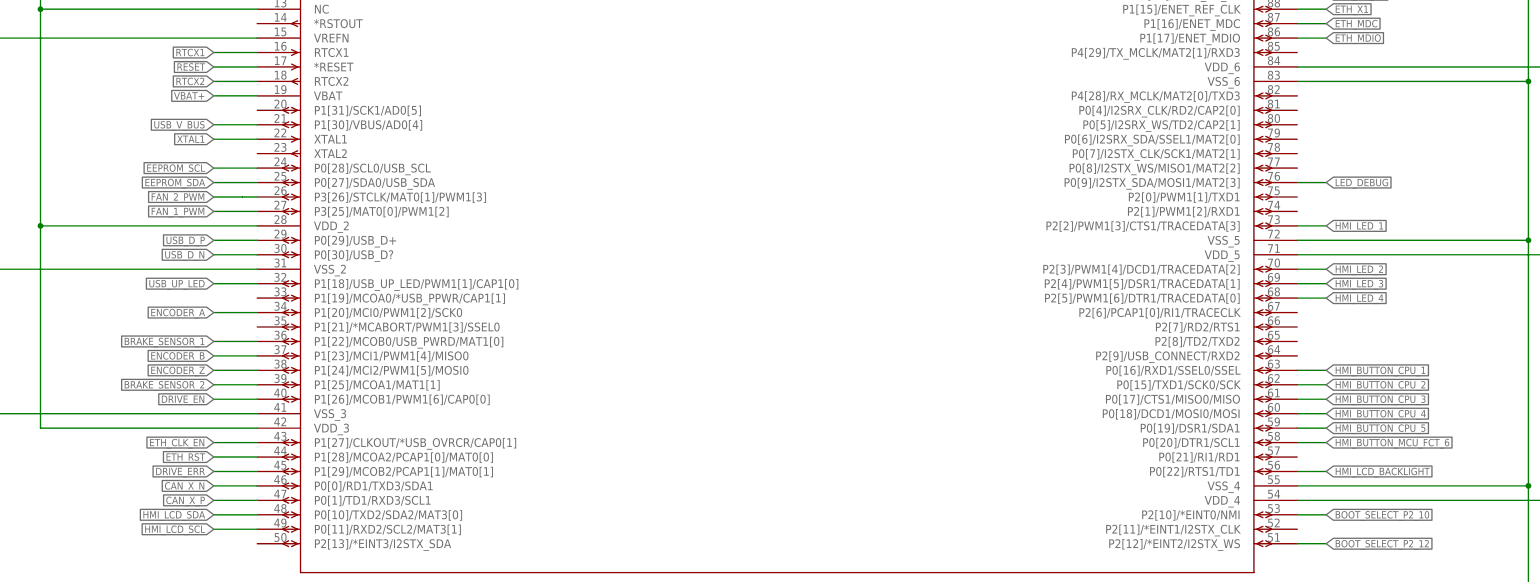
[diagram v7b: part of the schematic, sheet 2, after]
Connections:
- net BRAKE_SENSOR_1: now also U6.P1[22]/MCOB0/USB_PWRD/MAT1[0]; no longer U6.P0[4]/I2SRX_CLK/RD2/CAP2[0]
- net BRAKE_SENSOR_2: now also U6.P1[25]/MCOA1/MAT1[1]; no longer U6.P0[5]/I2SRX_WS/TD2/CAP2[1]
- net DRIVE_EN: now also U6.P1[26]/MCOB1/PWM1[6]/CAP0[0]; no longer U6.P0[6]/I2SRX_SDA/SSEL1/MAT2[0]
- net DRIVE_ERR: now also U6.P1[29]/MCOB2/PCAP1[1]/MAT0[1]; no longer U6.P0[7]/I2STX_CLK/SCK1/MAT2[1]
- net LED_DEBUG: now also U6.P0[9]/I2STX_SDA/MOSI1/MAT2[3]; no longer U6.P1[21]/*MCABORT/PWM1[3]/SSEL0
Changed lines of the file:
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@@
 <net name="BRAKE_SENSOR_1" class="0">
 <segment>
-<pinref part="U6" gate="A" pin="P0[4]/I2SRX_CLK/RD2/CAP2[0]"/>
-<wire x1="317.5" y1="182.88" x2="322.58" y2="182.88" width="0.1524" layer="91"/>
-<label x="322.58" y="182.88" size="1.27" layer="95" xref="yes"/>
+<label x="127" y="142.24" size="1.27" layer="95" rot="R180" xref="yes"/>
+<pinref part="U6" gate="A" pin="P1[22]/MCOB0/USB_PWRD/MAT1[0]"/>
+<wire x1="127" y1="142.24" x2="134.62" y2="142.24" width="0.1524" layer="91"/>
 </segment>
 </net>
 <net name="BRAKE_SENSOR_2" class="0">
 <segment>
-<pinref part="U6" gate="A" pin="P0[5]/I2SRX_WS/TD2/CAP2[1]"/>
-<wire x1="317.5" y1="180.34" x2="322.58" y2="180.34" width="0.1524" layer="91"/>
-<label x="322.58" y="180.34" size="1.27" layer="95" xref="yes"/>
+<label x="127" y="134.62" size="1.27" layer="95" rot="R180" xref="yes"/>
+<pinref part="U6" gate="A" pin="P1[25]/MCOA1/MAT1[1]"/>
+<wire x1="127" y1="134.62" x2="134.62" y2="134.62" width="0.1524" layer="91"/>
 </segment>
 </net>
@@
 <net name="DRIVE_EN" class="0">
 <segment>
-<pinref part="U6" gate="A" pin="P0[6]/I2SRX_SDA/SSEL1/MAT2[0]"/>
-<wire x1="317.5" y1="177.8" x2="322.58" y2="177.8" width="0.1524" layer="91"/>
-<label x="322.58" y="177.8" size="1.27" layer="95" xref="yes"/>
+<label x="127" y="132.08" size="1.27" layer="95" rot="R180" xref="yes"/>
+<pinref part="U6" gate="A" pin="P1[26]/MCOB1/PWM1[6]/CAP0[0]"/>
+<wire x1="127" y1="132.08" x2="134.62" y2="132.08" width="0.1524" layer="91"/>
 </segment>
 </net>
 <net name="DRIVE_ERR" class="0">
 <segment>
-<pinref part="U6" gate="A" pin="P0[7]/I2STX_CLK/SCK1/MAT2[1]"/>
-<wire x1="317.5" y1="175.26" x2="322.58" y2="175.26" width="0.1524" layer="91"/>
-<label x="322.58" y="175.26" size="1.27" layer="95" xref="yes"/>
+<label x="127" y="119.38" size="1.27" layer="95" rot="R180" xref="yes"/>
+<pinref part="U6" gate="A" pin="P1[29]/MCOB2/PCAP1[1]/MAT0[1]"/>
+<wire x1="127" y1="119.38" x2="134.62" y2="119.38" width="0.1524" layer="91"/>
 </segment>
 </net>
@@
 <net name="LED_DEBUG" class="1">
 <segment>
-<wire x1="134.62" y1="144.78" x2="127.254" y2="144.78" width="0.1524" layer="91"/>
-<pinref part="U6" gate="A" pin="P1[21]/*MCABORT/PWM1[3]/SSEL0"/>
-<label x="127" y="144.78" size="1.27" layer="95" rot="R180" xref="yes"/>
-</segment>
-<segment>
 <wire x1="358.14" y1="38.1" x2="343.916" y2="38.1" width="0.1524" layer="91"/>
 <label x="343.916" y="38.1" size="1.27" layer="95" rot="R180" xref="yes"/>
@@
 <wire x1="358.14" y1="40.64" x2="358.14" y2="38.1" width="0.1524" layer="91"/>
 </segment>
-</net>
+<segment>
+<label x="322.58" y="170.18" size="1.27" layer="95" xref="yes"/>
+<pinref part="U6" gate="A" pin="P0[9]/I2STX_SDA/MOSI1/MAT2[3]"/>
+<wire x1="317.5" y1="170.18" x2="322.58" y2="170.18" width="0.1524" layer="91"/>
+</segment>
+</net>
